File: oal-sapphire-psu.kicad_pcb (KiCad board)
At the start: 2 copper layers, 100 x 80 mm, 120 parts, among them P7 OUTPUT, T1 TALEMA-25VA/12V, X1 MOUNTING_HOLE, X2 MOUNTING_HOLE, X3 MOUNTING_HOLE, X4 MOUNTING_HOLE

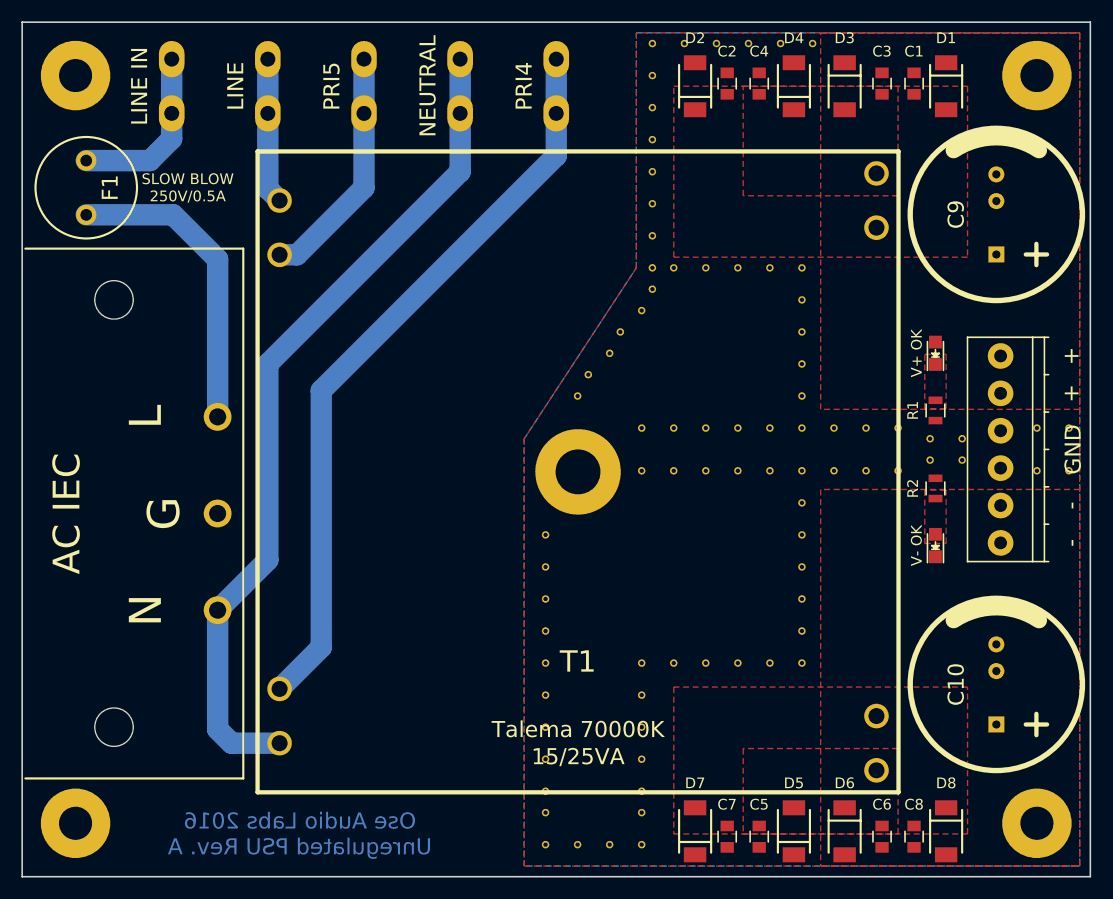
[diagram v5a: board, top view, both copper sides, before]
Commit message: simplified 120v only layout
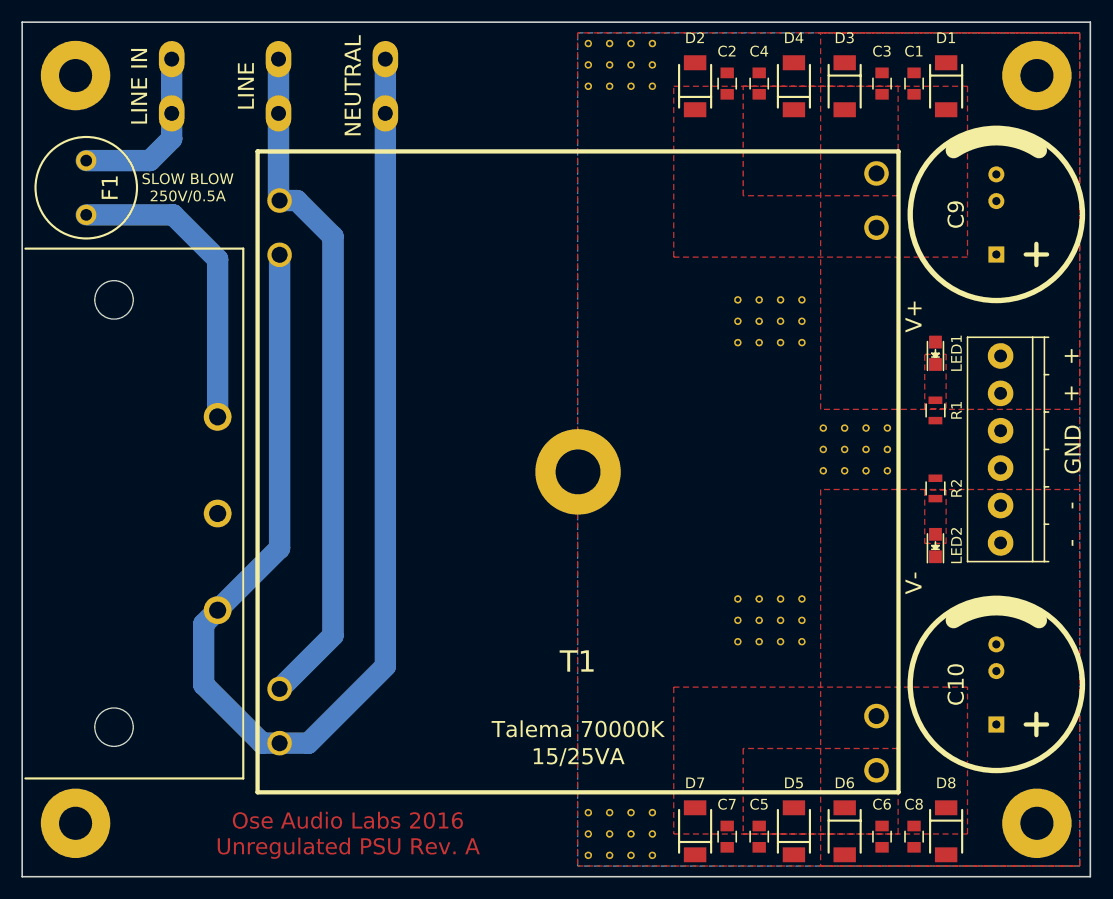
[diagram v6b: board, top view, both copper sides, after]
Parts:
- removed PRI4: PRIMARY_4, ose-audio-labs:FASTON_TAB
- removed PRI5: PRIMARY_5, ose-audio-labs:FASTON_TAB
- removed the REF** at (50.0, -17.0)
- removed VIA-GROUND (x84): TH-VIA, TH-VIA
- added REF**: TH-VIA, ose-audio-labs:TH-VIA, F.Cu at (73.0, -10.0)
- added REF**: TH-VIA, ose-audio-labs:TH-VIA, F.Cu at (81.0, 0.00)
- added REF**: TH-VIA, ose-audio-labs:TH-VIA, F.Cu at (79.0, 0.00)
- added REF**: TH-VIA, ose-audio-labs:TH-VIA, F.Cu at (79.0, 2.00)
- added REF**: TH-VIA, ose-audio-labs:TH-VIA, F.Cu at (79.0, -2.00)
- added REF**: TH-VIA, ose-audio-labs:TH-VIA, F.Cu at (81.0, -2.00)
- added REF**: TH-VIA, ose-audio-labs:TH-VIA, F.Cu at (75.0, -2.00)
- added REF**: TH-VIA, ose-audio-labs:TH-VIA, F.Cu at (77.0, -2.00)
- added REF**: TH-VIA, ose-audio-labs:TH-VIA, F.Cu at (77.0, 2.00)
- added REF**: TH-VIA, ose-audio-labs:TH-VIA, F.Cu at (75.0, 2.00)
- added REF**: TH-VIA, ose-audio-labs:TH-VIA, F.Cu at (77.0, 0.00)
- added REF**: TH-VIA, ose-audio-labs:TH-VIA, F.Cu at (71.0, -10.0)
- added REF**: TH-VIA, ose-audio-labs:TH-VIA, F.Cu at (75.0, 0.00)
- added REF**: TH-VIA, ose-audio-labs:TH-VIA, F.Cu at (67.0, 16.0)
- added REF**: TH-VIA, ose-audio-labs:TH-VIA, F.Cu at (67.0, 18.0)
- added REF**: TH-VIA, ose-audio-labs:TH-VIA, F.Cu at (69.0, 16.0)
- added REF**: TH-VIA, ose-audio-labs:TH-VIA, F.Cu at (69.0, 18.0)
- added REF**: TH-VIA, ose-audio-labs:TH-VIA, F.Cu at (71.0, 16.0)
- added REF**: TH-VIA, ose-audio-labs:TH-VIA, F.Cu at (71.0, 18.0)
- added REF**: TH-VIA, ose-audio-labs:TH-VIA, F.Cu at (73.0, 16.0)
- added REF**: TH-VIA, ose-audio-labs:TH-VIA, F.Cu at (73.0, 18.0)
- added REF**: TH-VIA, ose-audio-labs:TH-VIA, F.Cu at (67.0, -14.0)
- added REF**: TH-VIA, ose-audio-labs:TH-VIA, F.Cu at (69.0, -10.0)
- added REF**: TH-VIA, ose-audio-labs:TH-VIA, F.Cu at (67.0, -12.0)
- added REF**: TH-VIA, ose-audio-labs:TH-VIA, F.Cu at (69.0, -14.0)
- added REF**: TH-VIA, ose-audio-labs:TH-VIA, F.Cu at (71.0, -12.0)
- added REF**: TH-VIA, ose-audio-labs:TH-VIA, F.Cu at (69.0, -12.0)
- added REF**: TH-VIA, ose-audio-labs:TH-VIA, F.Cu at (71.0, -14.0)
- added REF**: TH-VIA, ose-audio-labs:TH-VIA, F.Cu at (73.0, -14.0)
- added REF**: TH-VIA, ose-audio-labs:TH-VIA, F.Cu at (73.0, -12.0)
- added REF**: TH-VIA, ose-audio-labs:TH-VIA, F.Cu at (53.0, -38.0)
- added REF**: TH-VIA, ose-audio-labs:TH-VIA, F.Cu at (53.0, -36.0)
- added REF**: TH-VIA, ose-audio-labs:TH-VIA, F.Cu at (53.0, -34.0)
- added REF**: TH-VIA, ose-audio-labs:TH-VIA, F.Cu at (67.0, -10.0)
- added REF**: TH-VIA, ose-audio-labs:TH-VIA, F.Cu at (55.0, -38.0)
- added REF**: TH-VIA, ose-audio-labs:TH-VIA, F.Cu at (55.0, -36.0)
- added REF**: TH-VIA, ose-audio-labs:TH-VIA, F.Cu at (57.0, -34.0)
- added REF**: TH-VIA, ose-audio-labs:TH-VIA, F.Cu at (55.0, -34.0)
- added REF**: TH-VIA, ose-audio-labs:TH-VIA, F.Cu at (57.0, -38.0)
- added REF**: TH-VIA, ose-audio-labs:TH-VIA, F.Cu at (57.0, -36.0)
- added REF**: TH-VIA, ose-audio-labs:TH-VIA, F.Cu at (59.0, -38.0)
- added REF**: TH-VIA, ose-audio-labs:TH-VIA, F.Cu at (59.0, -36.0)
- added REF**: TH-VIA, ose-audio-labs:TH-VIA, F.Cu at (59.0, -34.0)
- added REF**: TH-VIA, ose-audio-labs:TH-VIA, F.Cu at (57.0, 34.0)
- added REF**: TH-VIA, ose-audio-labs:TH-VIA, F.Cu at (73.0, 14.0)
- added REF**: TH-VIA, ose-audio-labs:TH-VIA, F.Cu at (55.0, 34.0)
- added REF**: TH-VIA, ose-audio-labs:TH-VIA, F.Cu at (53.0, 34.0)
- added REF**: TH-VIA, ose-audio-labs:TH-VIA, F.Cu at (53.0, 36.0)
- added REF**: TH-VIA, ose-audio-labs:TH-VIA, F.Cu at (55.0, 36.0)
- added REF**: TH-VIA, ose-audio-labs:TH-VIA, F.Cu at (57.0, 36.0)
- added REF**: TH-VIA, ose-audio-labs:TH-VIA, F.Cu at (59.0, 34.0)
- added REF**: TH-VIA, ose-audio-labs:TH-VIA, F.Cu at (59.0, 36.0)
- added REF**: TH-VIA, ose-audio-labs:TH-VIA, F.Cu at (59.0, 38.0)
- added REF**: TH-VIA, ose-audio-labs:TH-VIA, F.Cu at (57.0, 38.0)
- added REF**: TH-VIA, ose-audio-labs:TH-VIA, F.Cu at (55.0, 38.0)
- added REF**: TH-VIA, ose-audio-labs:TH-VIA, F.Cu at (71.0, 14.0)
- added REF**: TH-VIA, ose-audio-labs:TH-VIA, F.Cu at (53.0, 38.0)
- added REF**: TH-VIA, ose-audio-labs:TH-VIA, F.Cu at (69.0, 14.0)
- added REF**: TH-VIA, ose-audio-labs:TH-VIA, F.Cu at (67.0, 14.0)
- added REF**: TH-VIA, ose-audio-labs:TH-VIA, F.Cu at (81.0, 2.00)
- LED1: renamed from V+ OK; value V+_OK -> V+
- LED2: renamed from V- OK; value V-_OK -> V-
- P1: renamed from AC IEC; value IEC -> 120V AC
- P2: renamed from LINE IN; value LINE -> LINE IN
- P3: renamed from LINE; value SWITCHED_LINE -> LINE
- R1, R2: value 820R -> 680R
- moved P4 7.00 mm to (34.0, -34.0), turned to 90 degrees
- moved P3 1.00 mm to (24.0, -34.0), turned to 90 degrees
- turned P2 to 90 degrees
- renumbered NEUTRAL to P4
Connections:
- P3 pad 1: Net-(P6-Pad1) -> Net-(P3-Pad1)
- T1 pad 4: Net-(P4-Pad1) -> Net-(P3-Pad1)
- T1 pad 5: Net-(P5-Pad1) -> NEUTRAL
- T1 pad 6: Net-(P6-Pad1) -> Net-(P3-Pad1)
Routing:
- net Net-(P4-Pad1): track 69.7 -> 0.00 mm
- net Net-(P3-Pad1): track 0.00 -> 64.1 mm
- net NEUTRAL: track 78.5 -> 122.3 mm
- net Net-(P5-Pad1): track 22.5 -> 0.00 mm
- net Net-(P6-Pad1): track 13.7 -> 0.00 mm
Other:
- board text added: "DANGER HIGH VOLTAGE!"
- board text removed: "120V: LINE-PRI4 NEUTRAL-PRI5 240V: PRI5-PRI4"

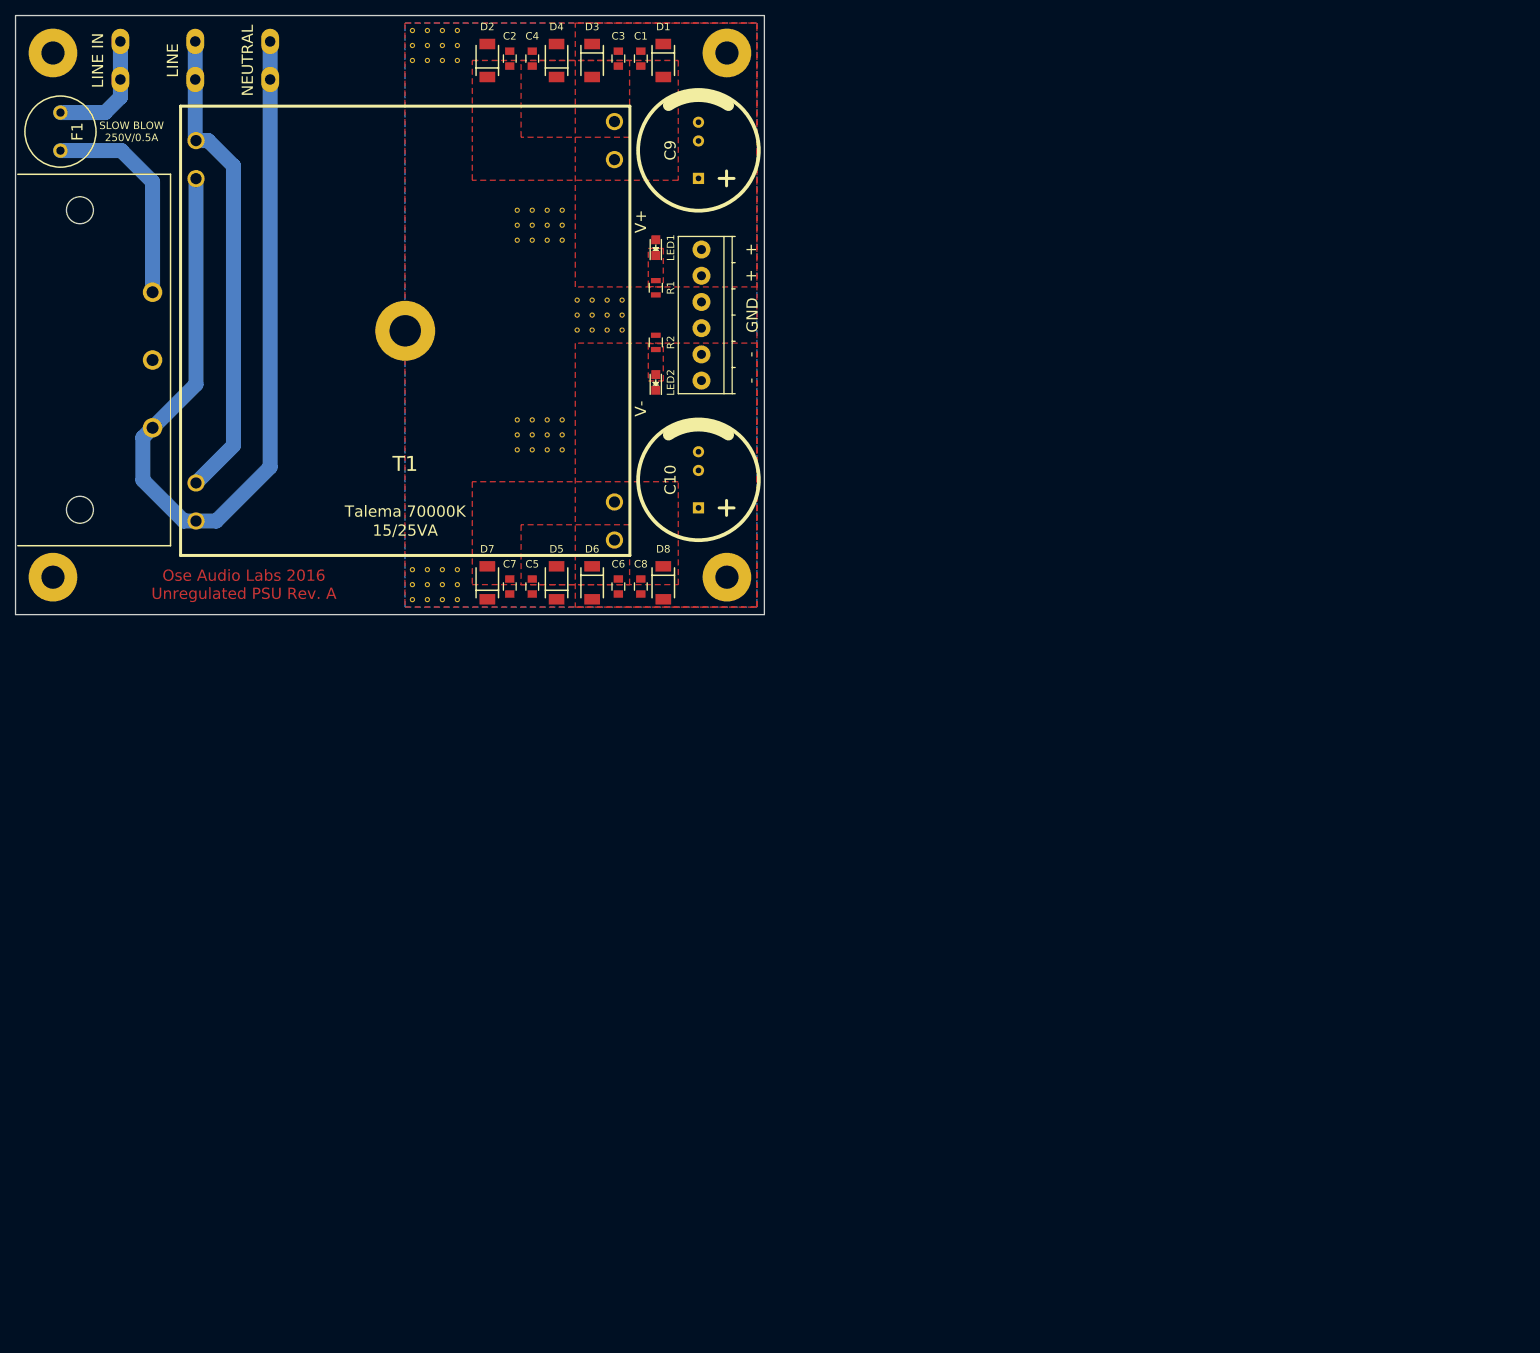
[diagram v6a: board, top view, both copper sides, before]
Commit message: 120v only
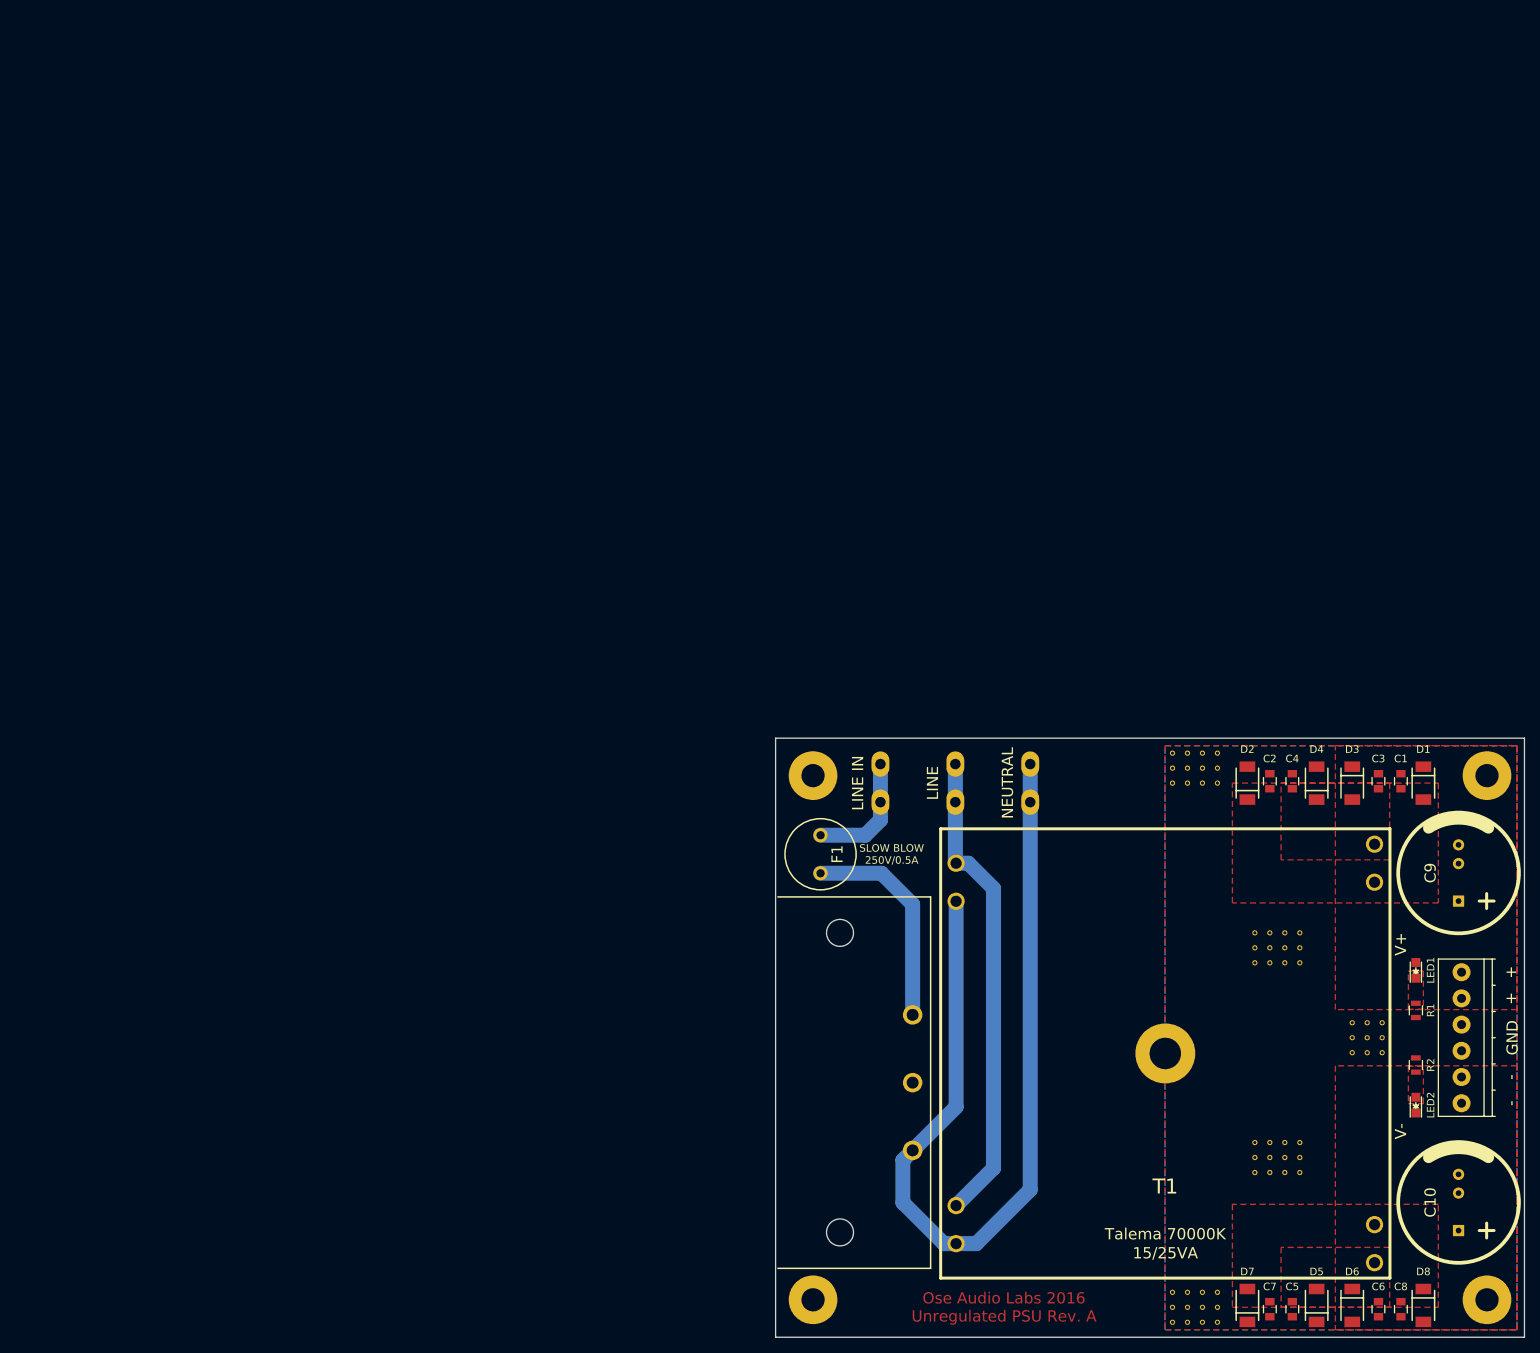
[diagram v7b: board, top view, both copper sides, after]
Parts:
- removed the REF** at (75.0, -2.00)
- removed the REF** at (75.0, 2.00)
- removed the REF** at (75.0, 0.00)
- moved C1 140.1 mm to (185.0, 62.2)
- moved C2 140.1 mm to (167.5, 62.2)
- moved C3 140.1 mm to (182.0, 62.2)
- moved C4 140.1 mm to (170.5, 62.2)
- moved C5 140.1 mm to (170.5, 132.8)
- moved C6 140.1 mm to (182.0, 132.8)
- moved C7 140.1 mm to (167.5, 132.8)
- moved C8 140.1 mm to (185.0, 132.8)
- moved D1 140.1 mm to (188.0, 62.5)
- moved D2 140.1 mm to (164.5, 62.5)
- moved D3 140.1 mm to (178.5, 62.5)
- moved D4 140.1 mm to (173.8, 62.5)
- moved D5 140.1 mm to (173.8, 132.2)
- moved D6 140.1 mm to (178.5, 132.2)
- moved D7 140.1 mm to (164.5, 132.2)
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
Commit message: rev a fab
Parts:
- C9: footprint ose-audio-labs:25V-LYTIC-7.5-5-16mm -> 25V-LYTIC-7.5-5-16mm
